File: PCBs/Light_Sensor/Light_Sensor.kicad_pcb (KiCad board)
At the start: 2 copper layers, 5 parts, among them J2 Conn_01x03

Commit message: latest PCBs
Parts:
- D1: footprint Artisyn_Components:DIODE_0805 -> Diode_THT:D_DO-15_P5.08mm_Vertical_AnodeUp
- moved D1 5.08 mm to (149.9, 78.7)
- moved H1 2.54 mm to (147.3, 73.7)
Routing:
- net VCC: track 5.39 -> 10.2 mm
- net Net-(D1-A): track 9.22 -> 9.92 mm
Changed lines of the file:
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@@
     (pad "" np_thru_hole circle (at 0 0) (size 2.7 2.7) (drill 2.7) (layers "*.Cu" "*.Mask"))
   )
-  (footprint "Artisyn_Components:DIODE_0805" (layer "F.Cu")
-    (at 149.86 83.82 -90)
-    (tags "TEMD7000X01 ")
+  (footprint "Diode_THT:D_DO-15_P5.08mm_Vertical_AnodeUp" (layer "F.Cu")
+    (at 149.86 78.74 -90)
+    (descr "Diode, DO-15 series, Axial, Vertical, pin pitch=5.08mm, , length*diameter=7.6*3.6mm^2, , http://www.diodes.com/_files/packages/DO-15.pdf")
+    (tags "Diode DO-15 series Axial Vertical pin pitch 5.08mm  length 7.6mm diameter 3.6mm")
     (property "Sheetfile" "Light_Sensor.kicad_sch")
     (property "Sheetname" "")
     (property "ki_description" "Photodiode")
     (property "ki_keywords" "photodiode diode opto")
-    (attr smd)
-    (fp_text reference "D1" (at 0 0 -90 unlocked) (layer "F.SilkS")
-        (effects (font (size 1 1) (thickness 0.15)))
-    )
-    (fp_text value "D_Photo" (at 0 -2.54 -90 unlocked) (layer "F.Fab")
-        (effects (font (size 1 1) (thickness 0.15)))
-    )
-    (fp_text user "${REFERENCE}" (at 0 0 -90 unlocked) (layer "F.Fab")
-        (effects (font (size 1 1) (thickness 0.15)))
-    )
-    (fp_line (start -1.4605 -0.9779) (end 1.4605 -0.9779)
-      (stroke (width 0.1524) (type solid)) (layer "F.CrtYd"))
-    (fp_line (start -1.4605 0.9779) (end -1.4605 -0.9779)
-      (stroke (width 0.1524) (type solid)) (layer "F.CrtYd"))
-    (fp_line (start 1.4605 -0.9779) (end 1.4605 0.9779)
-      (stroke (width 0.1524) (type solid)) (layer "F.CrtYd"))
-    (fp_line (start 1.4605 0.9779) (end -1.4605 0.9779)
-      (stroke (width 0.1524) (type solid)) (layer "F.CrtYd"))
-    (fp_line (start -1.0033 -0.7239) (end -1.0033 0.7239)
-      (stroke (width 0.0254) (type solid)) (layer "F.Fab"))
-    (fp_line (start -1.0033 -0.7239) (end -1.0033 0.7239)
-      (stroke (width 0.0254) (type solid)) (layer "F.Fab"))
-    (fp_line (start -1.0033 0.7239) (end -0.1905 0.7239)
-      (stroke (width 0.0254) (type solid)) (layer "F.Fab"))
-    (fp_line (start -1.0033 0.7239) (end 1.0033 0.7239)
-      (stroke (width 0.0254) (type solid)) (layer "F.Fab"))
-    (fp_line (start -0.1905 -0.7239) (end -1.0033 -0.7239)
-      (stroke (width 0.0254) (type solid)) (layer "F.Fab"))
-    (fp_line (start -0.1905 0.7239) (end -0.1905 -0.7239)
-      (stroke (width 0.0254) (type solid)) (layer "F.Fab"))
-    (fp_line (start 0.1905 -0.7239) (end 0.1905 0.7239)
-      (stroke (width 0.0254) (type solid)) (layer "F.Fab"))
-    (fp_line (start 0.1905 0.7239) (end 1.0033 0.7239)
-      (stroke (width 0.0254) (type solid)) (layer "F.Fab"))
-    (fp_line (start 1.0033 -0.7239) (end -1.0033 -0.7239)
-      (stroke (width 0.0254) (type solid)) (layer "F.Fab"))
-    (fp_line (start 1.0033 -0.7239) (end 0.1905 -0.7239)
-      (stroke (width 0.0254) (type solid)) (layer "F.Fab"))
-    (fp_line (start 1.0033 0.7239) (end 1.0033 -0.7239)
-      (stroke (width 0.0254) (type solid)) (layer "F.Fab"))
-    (fp_line (start 1.0033 0.7239) (end 1.0033 -0.7239)
-      (stroke (width 0.0254) (type solid)) (layer "F.Fab"))
-    (pad "1" smd rect (at -0.6985 0 270) (size 1.016 1.4478) (layers "F.Cu" "F.Paste" "F.Mask")
+    (attr through_hole)
+    (fp_text reference "D1" (at 2.54 -2.92 -90) (layer "F.SilkS")
+        (effects (font (size 1 1) (thickness 0.15)))
+    )
+    (fp_text value "D_Photo" (at 2.54 2.92 -90) (layer "F.Fab")
+        (effects (font (size 1 1) (thickness 0.15)))
+    )
+    (fp_text user "A" (at 3.18 1.2 -90) (layer "F.SilkS")
+        (effects (font (size 1 1) (thickness 0.15)))
+    )
+    (fp_text user "A" (at 3.18 1.2 -90) (layer "F.Fab")
+        (effects (font (size 1 1) (thickness 0.15)))
+    )
+    (fp_text user "${REFERENCE}" (at 2.54 -2.92 -90) (layer "F.Fab")
+        (effects (font (size 1 1) (thickness 0.15)))
+    )
+    (fp_line (start 1.92 0) (end 3.58 0)
+      (stroke (width 0.12) (type solid)) (layer "F.SilkS"))
+    (fp_circle (center 0 0) (end 1.92 0)
+      (stroke (width 0.12) (type solid)) (fill none) (layer "F.SilkS"))
+    (fp_line (start -2.05 -2.05) (end -2.05 2.05)
+      (stroke (width 0.05) (type solid)) (layer "F.CrtYd"))
+    (fp_line (start -2.05 2.05) (end 6.53 2.05)
+      (stroke (width 0.05) (type solid)) (layer "F.CrtYd"))
+    (fp_line (start 6.53 -2.05) (end -2.05 -2.05)
+      (stroke (width 0.05) (type solid)) (layer "F.CrtYd"))
+    (fp_line (start 6.53 2.05) (end 6.53 -2.05)
+      (stroke (width 0.05) (type solid)) (layer "F.CrtYd"))
+    (fp_line (start 0 0) (end 5.08 0)
+      (stroke (width 0.1) (type solid)) (layer "F.Fab"))
+    (fp_circle (center 0 0) (end 1.8 0)
+      (stroke (width 0.1) (type solid)) (fill none) (layer "F.Fab"))
+    (pad "1" thru_hole rect (at 0 0 270) (size 2.4 2.4) (drill 1.2) (layers "*.Cu" "*.Mask")
       (net 1 "VCC") (pinfunction "K") (pintype "passive"))
-    (pad "2" smd rect (at 0.6985 0 270) (size 1.016 1.4478) (layers "F.Cu" "F.Paste" "F.Mask")
+    (pad "2" thru_hole oval (at 5.08 0 270) (size 2.4 2.4) (drill 1.2) (layers "*.Cu" "*.Mask")
       (net 2 "Net-(D1-A)") (pinfunction "A") (pintype "passive"))
-    (zone (net 0) (net_name "") (layer "F.Cu") (hatch full 0.508)
-      (connect_pads (clearance 0))
-      (min_thickness 0.254) (filled_areas_thickness no)
-      (keepout (tracks not_allowed) (vias not_allowed) (pads allowed) (copperpour not_allowed) (footprints allowed))
-      (fill (thermal_gap 0.508) (thermal_bridge_width 0.508))
-      (polygon
-        (pts
-          (xy 150.5331 83.6803)
-          (xy 150.5331 83.9597)
-          (xy 149.1869 83.9597)
-          (xy 149.1869 83.6803)
-        )
-      )
+    (model "${KICAD6_3DMODEL_DIR}/Diode_THT.3dshapes/D_DO-15_P5.08mm_Vertical_AnodeUp.wrl"
+      (offset (xyz 0 0 0))
+      (scale (xyz 1 1 1))
+      (rotate (xyz 0 0 0))
     )
   )
   (footprint "MountingHole:MountingHole_2.7mm" (layer "F.Cu")
-    (at 147.32 76.2)
+    (at 147.32 73.66)
     (descr "Mounting Hole 2.7mm, no annular")
     (tags "mounting hole 2.7mm no annular")
@@
     )
   )
-  (segment (start 149.86 83.1215) (end 148.0185 83.1215) (width 0.25) (layer "F.Cu") (net 1))
-  (segment (start 148.0185 83.1215) (end 147.28 83.86) (width 0.25) (layer "F.Cu") (net 1))
-  (segment (start 147.28 83.86) (end 144.78 83.86) (width 0.25) (layer "F.Cu") (net 1))
+  (segment (start 144.78 83.86) (end 144.78 78.74) (width 0.25) (layer "F.Cu") (net 1))
+  (segment (start 144.78 78.74) (end 149.86 78.74) (width 0.25) (layer "F.Cu") (net 1))
+  (segment (start 149.86 83.82) (end 149.86 87.9875) (width 0.25) (layer "F.Cu") (net 2))
   (segment (start 149.86 87.9875) (end 148.9475 87.9875) (width 0.25) (layer "F.Cu") (net 2))
   (segment (start 147.32 86.36) (end 144.78 86.36) (width 0.25) (layer "F.Cu") (net 2))
-  (segment (start 149.86 87.9875) (end 149.86 84.5185) (width 0.25) (layer "F.Cu") (net 2))
   (segment (start 148.9475 87.9875) (end 147.32 86.36) (width 0.25) (layer "F.Cu") (net 2))
   (segment (start 147.28 88.86) (end 144.78 88.86) (width 0.25) (layer "F.Cu") (net 3))

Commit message: i
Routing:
- net VCC: track 10.2 -> 29.0 mm, vias 0 -> 5
- net (no net): track 0.00 -> 9.44 mm
- net GND: track 5.47 -> 12.2 mm, vias 0 -> 3
- added copper zone on B.Cu, net GND
- added copper zone on F.Cu, net GND
- added copper zone on B.Cu, net VCC
- added copper zone on F.Cu, net VCC
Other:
- board outline added: 10.2 x 30.5 mm
- board text added: "Team 8 Light Sensor"
- board text added: "VCC"

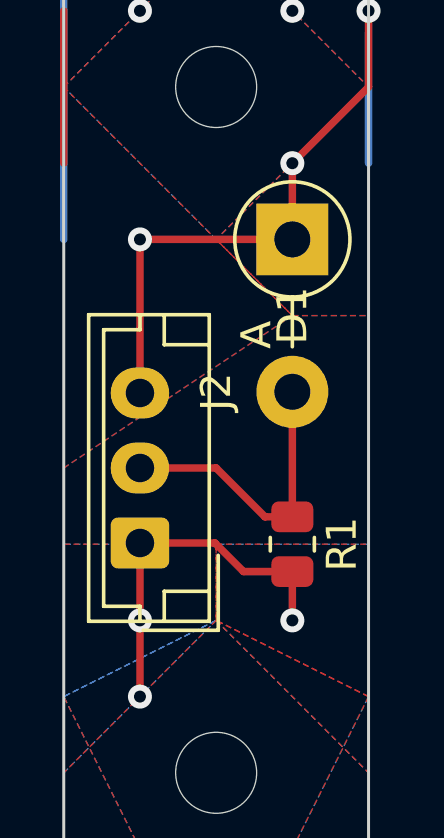
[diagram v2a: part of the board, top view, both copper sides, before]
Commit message: fixed PCB layout and updated gbr and drl files
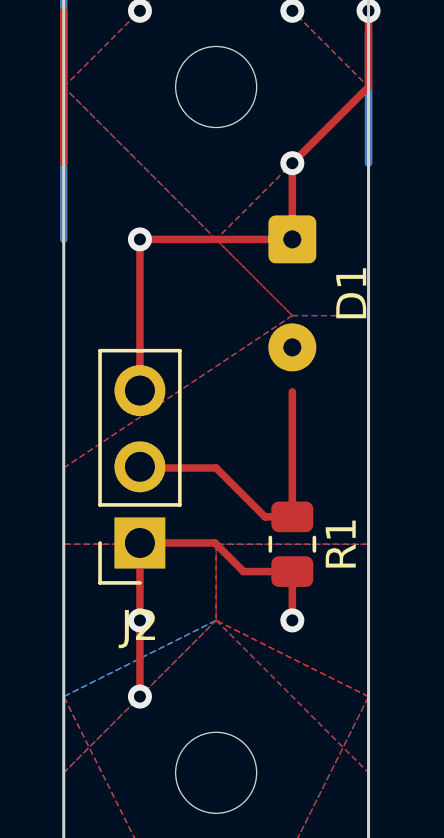
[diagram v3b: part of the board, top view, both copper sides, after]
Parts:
- D1: footprint Diode_THT:D_DO-15_P5.08mm_Vertical_AnodeUp -> Connector_Wire:SolderWire-0.1sqmm_1x02_P3.6mm_D0.4mm_OD1mm
- J2: footprint Connector_JST:JST_EH_B3B-EH-A_1x03_P2.50mm_Vertical -> Connector_PinSocket_2.54mm:PinSocket_1x03_P2.54mm_Vertical
- turned J2 to 180 degrees
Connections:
- net VCC renamed 3.3V

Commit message: fixed trace
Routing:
- net Net-(D1-A): track 9.92 -> 11.4 mm
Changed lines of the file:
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@@
   (segment (start 142.24 71.12) (end 142.24 76.2) (width 0.25) (layer "F.Cu") (net 0))
   (segment (start 152.4 76.2) (end 152.4 71.845) (width 0.25) (layer "B.Cu") (net 0))
-  (segment (start 149.86 83.82) (end 149.86 87.9875) (width 0.25) (layer "F.Cu") (net 1))
+  (segment (start 149.86 82.34) (end 149.86 87.9875) (width 0.25) (layer "F.Cu") (net 1))
   (segment (start 149.86 87.9875) (end 148.9475 87.9875) (width 0.25) (layer "F.Cu") (net 1))
   (segment (start 147.32 86.36) (end 144.78 86.36) (width 0.25) (layer "F.Cu") (net 1))

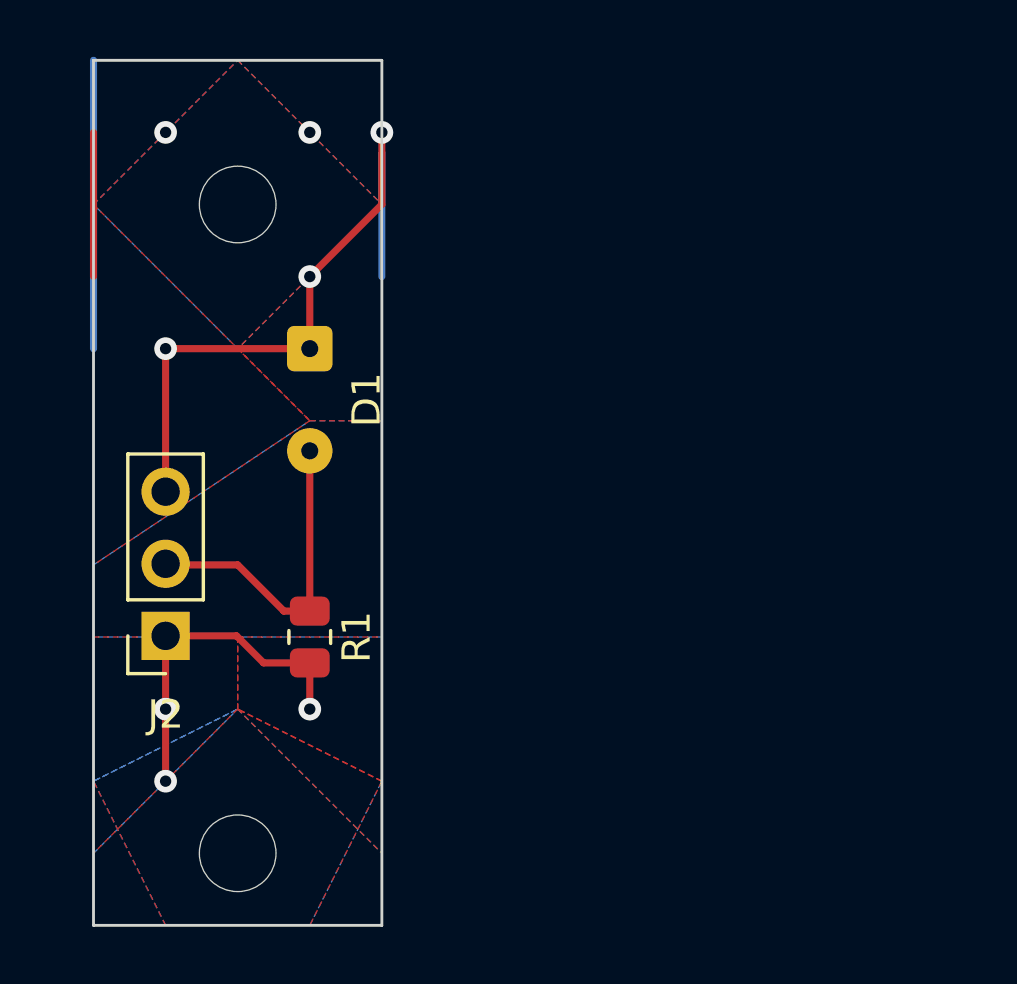
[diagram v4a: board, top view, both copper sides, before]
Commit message: finished Main and Light Sensor PCBs
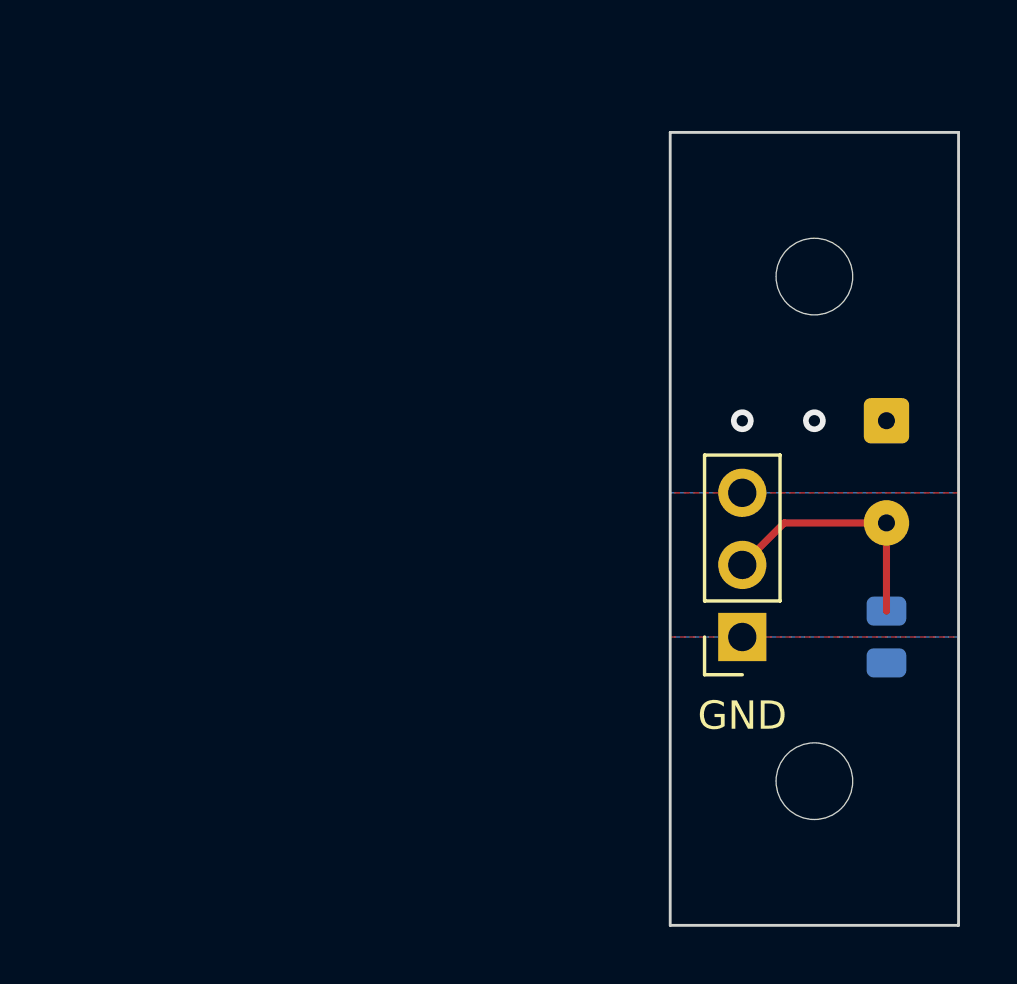
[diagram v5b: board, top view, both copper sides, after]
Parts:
- removed J2: Conn_01x03, Connector_PinSocket_2.54mm:PinSocket_1x03_P2.54mm_Vertical
- added GND: Conn_01x03, Connector_PinSocket_2.54mm:PinSocket_1x03_P2.54mm_Vertical, F.Cu at (165.1, 88.9)
- R1: moved to B.Cu
- moved D1 20.5 mm to (170.2, 81.3)
- moved H1 20.5 mm to (167.6, 76.2)
- moved H2 20.5 mm to (167.6, 94.0)
- moved R1 20.3 mm to (170.2, 88.9)
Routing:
- net 3.3V: track 29.0 -> 0.00 mm, vias 5 -> 2
- net GND: track 12.2 -> 0.00 mm, vias 3 -> 0
- net (no net): track 9.44 -> 0.00 mm
- net Net-(D1-A): track 11.4 -> 8.80 mm
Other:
- board size 10.2 x 30.5 mm -> 10.2 x 27.9 mm
- board text removed: "Team 8 Light Sensor"
- board text removed: "VCC"
